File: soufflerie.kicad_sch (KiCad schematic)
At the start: 68 parts, among them IC1 BMP390, IC2 SDP31, IC3 LM3940IMP-3.3, J1 MicroSD_Connector_503182-1852, J2 USB-C_12pin, J3 CON05, J4 CON05, J5 DB9_Male, J6 CON04, J7 CON05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

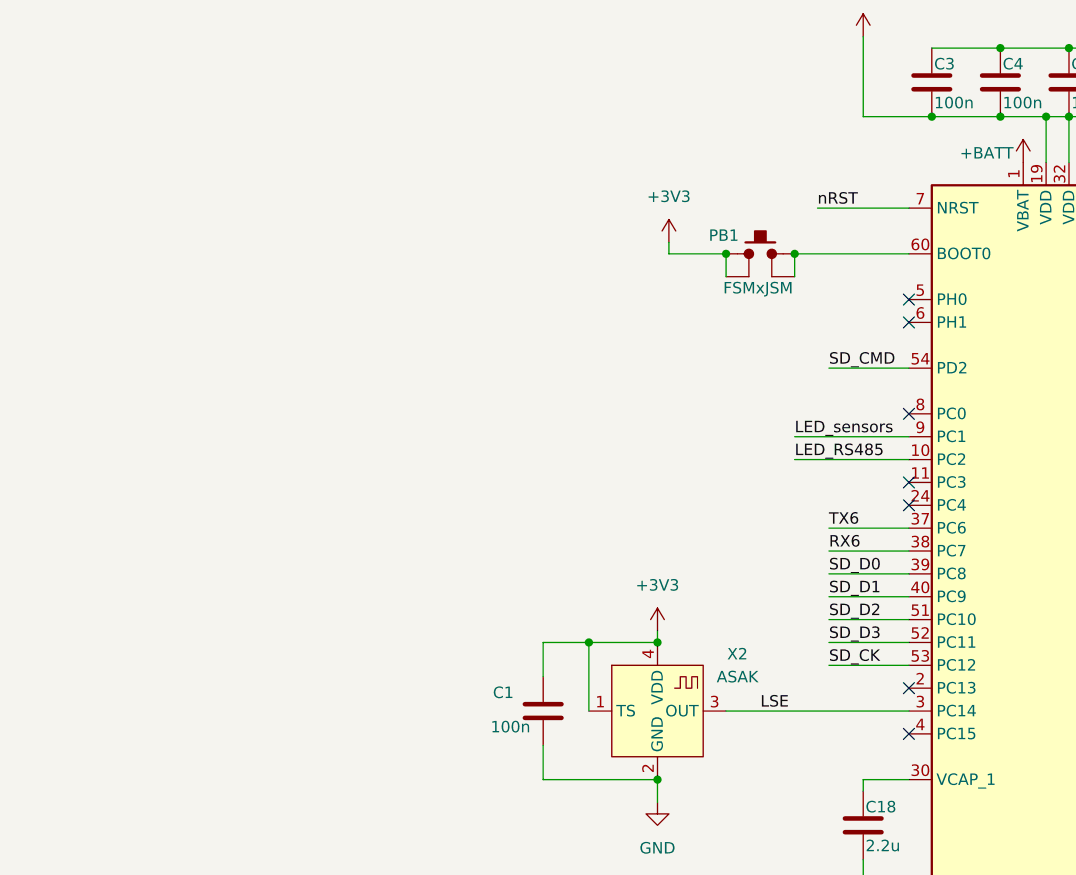
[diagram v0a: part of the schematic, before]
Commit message: Add HSE oscillator
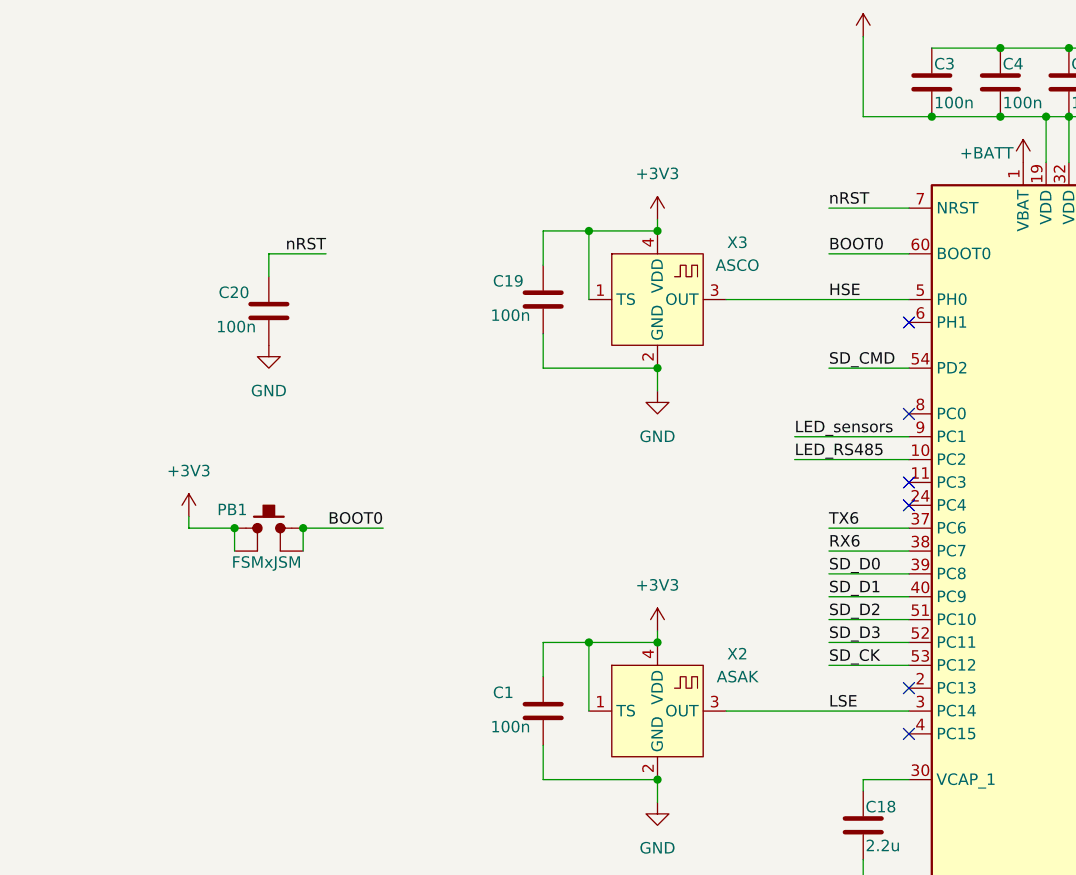
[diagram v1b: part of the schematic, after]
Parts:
- added C19, C20: 100n, Capacitor_SMD:C_0603_1608Metric, symbol Device:C
- added X3: ASCO, _Misc_GRZ:Osc_ASCO, symbol _GRZ_Misc:ASCO
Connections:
- net +3V3: now also C19.1, X3.1 (TS), X3.4 (VDD)
- net GND: now also C19.2, C20.2, X3.2 (GND)
- net nRST: now also C20.1
- net BOOT0: now reaches PB1.3, PB1.4, U3.60 (BOOT0)
- net HSE: now reaches U3.5 (PH0)
- net HSE: now also X3.3 (OUT)
- no-connect marks 31 -> 30
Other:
- moved on the sheet: PB1

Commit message: select DB9 footprint
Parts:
- J5: footprint Connector_Dsub:DSUB-9_Male_Horizontal_P2.77x2.54mm_EdgePinOffset9.40mm -> Connector_Dsub:DSUB-9_Male_Horizontal_P2.77x2.84mm_EdgePinOffset7.70mm_Housed_MountingHolesOffset9.12mm
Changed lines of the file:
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@@
 			)
 		)
-		(property "Footprint" "Connector_Dsub:DSUB-9_Male_Horizontal_P2.77x2.54mm_EdgePinOffset9.40mm"
+		(property "Footprint" "Connector_Dsub:DSUB-9_Male_Horizontal_P2.77x2.84mm_EdgePinOffset7.70mm_Housed_MountingHolesOffset9.12mm"
 			(at 278.13 247.65 0)
 			(effects

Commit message: routage
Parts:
- removed D2, D3, D4: LED, LED_SMD:LED_0603_1608Metric, symbol Device:LED
- removed R7, R8, R9: 500, Resistor_SMD:R_0603_1608Metric, symbol Device:R
- added H1, H2, H3, H4: MountingHole, MountingHole:MountingHole_3.2mm_M3, symbol Mechanical:MountingHole
- added H5, H6: MountingHole, MountingHole:MountingHole_2.2mm_M2, symbol Mechanical:MountingHole
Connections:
- net RS485A: now reaches J5.3, R12.2, R14.1, U2.6 (A)
- net RS485B: now reaches J5.8, R12.1, R13.2, U2.7 (B)
- net LED_RS485: no longer names the net of U3.10 (PC2)
- net LED_SD: no longer names the net of U3.41 (PA8)
- net LED_sensors: no longer names the net of U3.9 (PC1)
- net USB_DM renamed USB_N
- net USB_DP renamed USB_P
- no-connect marks 30 -> 33
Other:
- moved on the sheet: D5, D6, R10, R11

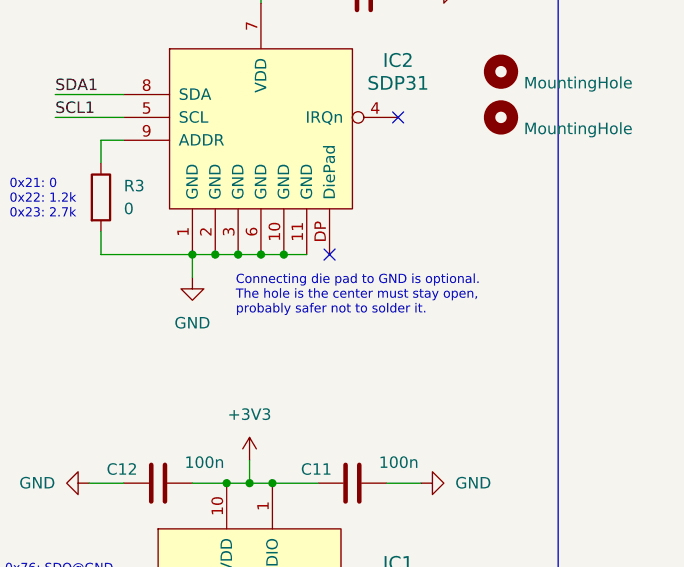
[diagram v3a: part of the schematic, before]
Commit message: connect SDP31 DIE pad
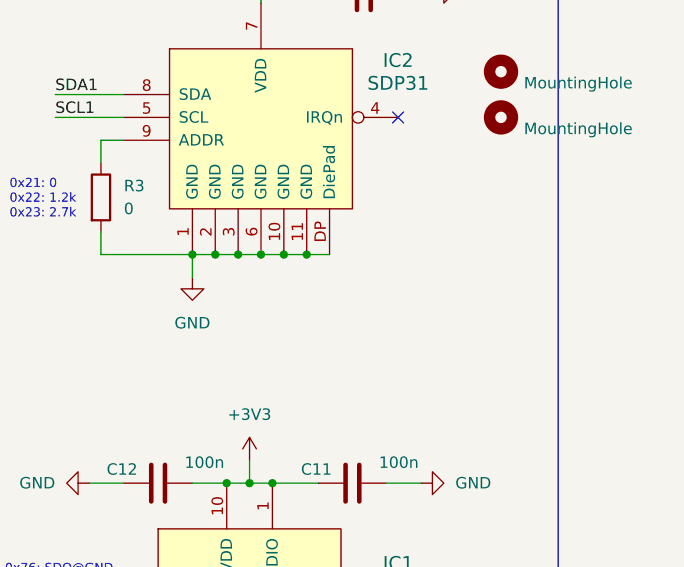
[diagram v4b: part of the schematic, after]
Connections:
- net GND: now also IC2.DP (DiePad)
- no-connect marks 33 -> 32
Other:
- note removed: "Connecting die pad to GND is optional. The hole is the center must stay open, probably safer not to solder it."
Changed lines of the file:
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@@
 	)
 	(junction
+		(at 375.92 60.96)
+		(diameter 0)
+		(color 0 0 0 0)
+	)
+	(junction
 		(at 238.76 231.14)
 		(diameter 0)
@@
 	)
 	(no_connect
-		(at 378.46 60.96)
-	)
-	(no_connect
 		(at 245.11 74.93)
 	)
@@
 	(wire
 		(pts
+			(xy 375.92 60.96) (xy 378.46 60.96)
+		)
+		(stroke
+			(width 0)
+			(type default)
+		)
+	)
+	(wire
+		(pts
 			(xy 132.08 36.83) (xy 139.7 36.83)
 		)
@@
 		)
 	)
-	(text "Connecting die pad to GND is optional.\nThe hole is the center must stay open,\nprobably safer not to solder it."
-		(exclude_from_sim no)
-		(at 368.046 65.532 0)
-		(effects
-			(font
-				(size 1.016 1.016)
-			)
-			(justify left)
-		)
-	)
